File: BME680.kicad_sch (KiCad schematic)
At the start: 19 parts, among them IC1 BME680, J3 HEADER-1X770MIL, Q1 BSS138, U3 AP2112K-3.3

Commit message: added Arduino UNO R4 in root sheet
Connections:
- net D6 renamed CS
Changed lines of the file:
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@@
 		)
 	)
-	(hierarchical_label "D6"
+	(hierarchical_label "CS"
 		(shape input)
 		(at 68.58 133.35 180)

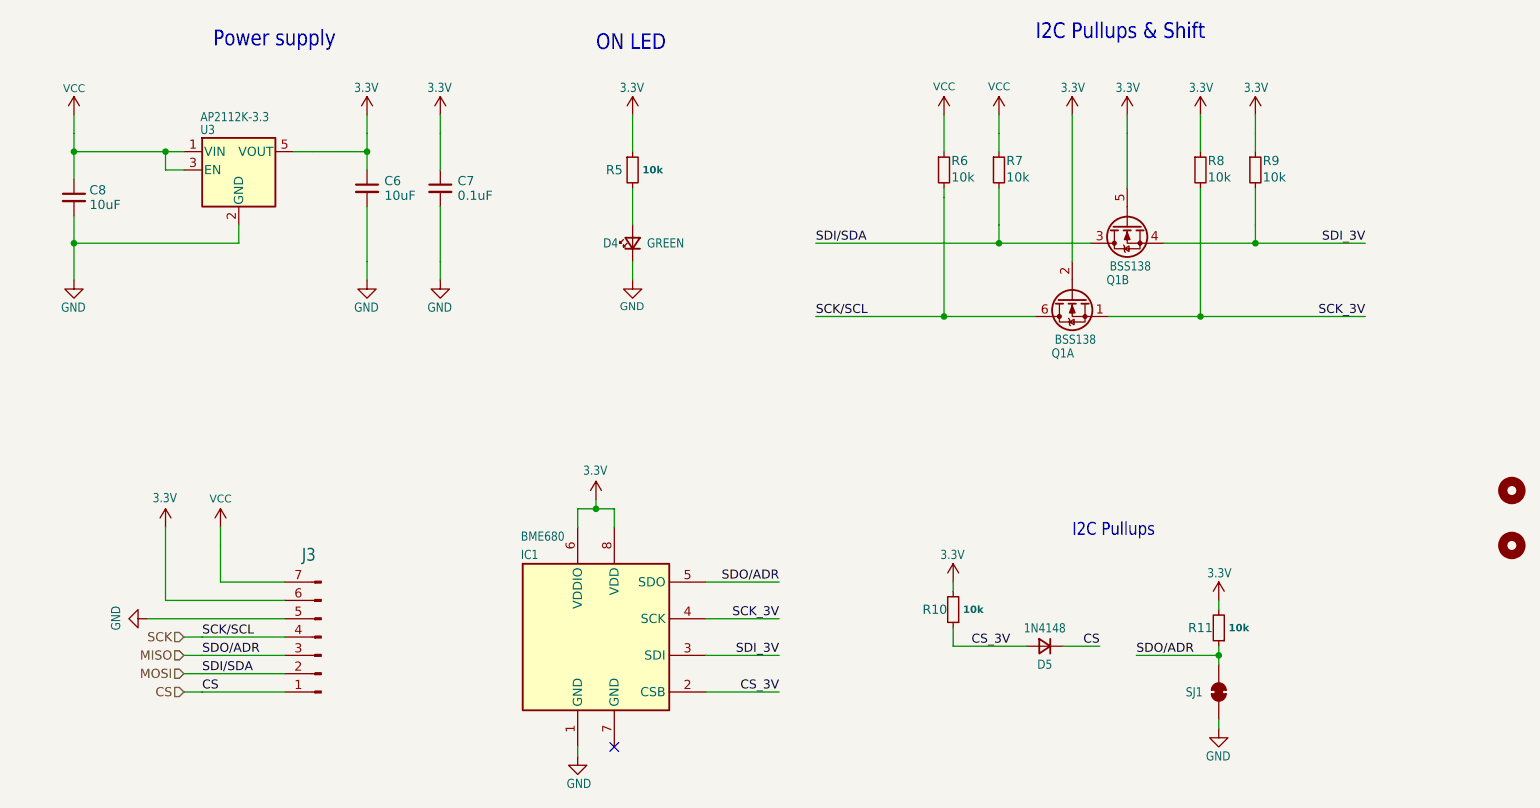
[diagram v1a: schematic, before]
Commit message: added pyrano, anemo, AM2315C, power supply, LEDs, switch and FPC connector in schematic
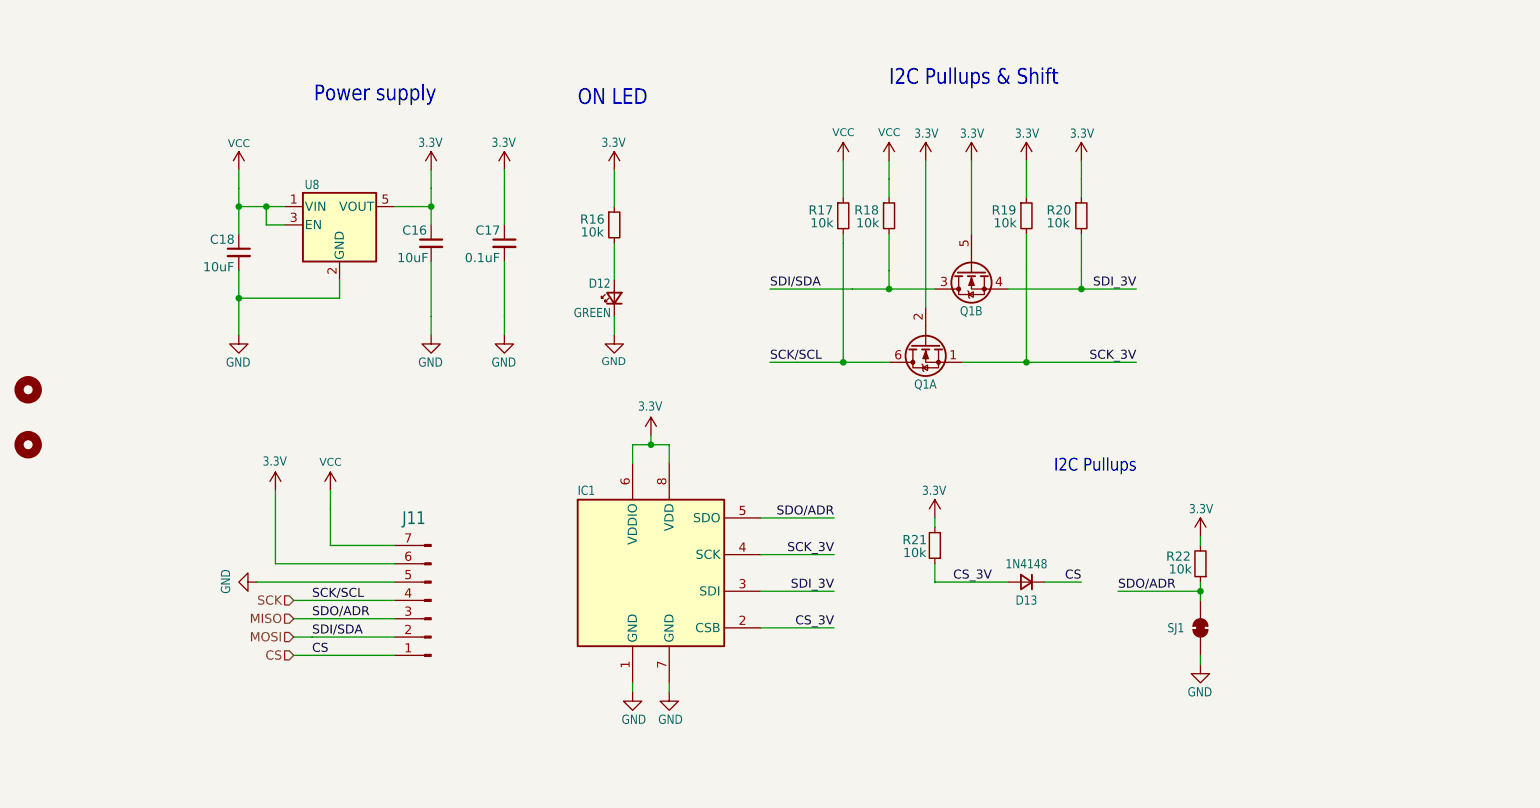
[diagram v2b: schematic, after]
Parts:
- C16: renamed from C6; Componant package type C_0805 -> (none); Component package type (none) -> C_0805
- C17: renamed from C7; Componant package type C_0603 -> (none); Component package type (none) -> C_0603
- C18: renamed from C8; Componant package type C_0805 -> (none); Component package type (none) -> C_0805
- D12: renamed from D4; Componant package type LED_0603 -> (none); Component package type (none) -> LED_0603
- D13: renamed from D5; Componant package type SOD-323 -> (none); Component package type (none) -> SOD-323
- IC1: Componant package type / -> (none)
- J11: renamed from J3; Componant package type / -> (none)
- Q1: Componant package type SOT-363 -> (none); Component package type (none) -> SOT-363
- R16: renamed from R5; Componant package type R_0603 -> (none); Component package type (none) -> R_0603
- R17: renamed from R6; Componant package type R_0603 -> (none); Component package type (none) -> R_0603
- R18: renamed from R7; Componant package type R_0603 -> (none); Component package type (none) -> R_0603
- R19: renamed from R8; Componant package type R_0603 -> (none); Component package type (none) -> R_0603
- R20: renamed from R9; Componant package type R_0603 -> (none); Component package type (none) -> R_0603
- R21: renamed from R10; Componant package type R_0603 -> (none); Component package type (none) -> R_0603
- R22: renamed from R11; Componant package type R_0603 -> (none); Component package type (none) -> R_0603
- U8: renamed from U3; Componant package type SOT-25 -> (none); Component package type (none) -> SOT-25
- renumbered U$3 to U$7, U$4 to U$8
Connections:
- net GND: now also IC1.7 (GND)
- no-connect marks 1 -> 0
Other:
- moved on the sheet: C16, C17, C18, D12, D13, IC1, J11, Q1A, Q1B, R16, R17, R18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

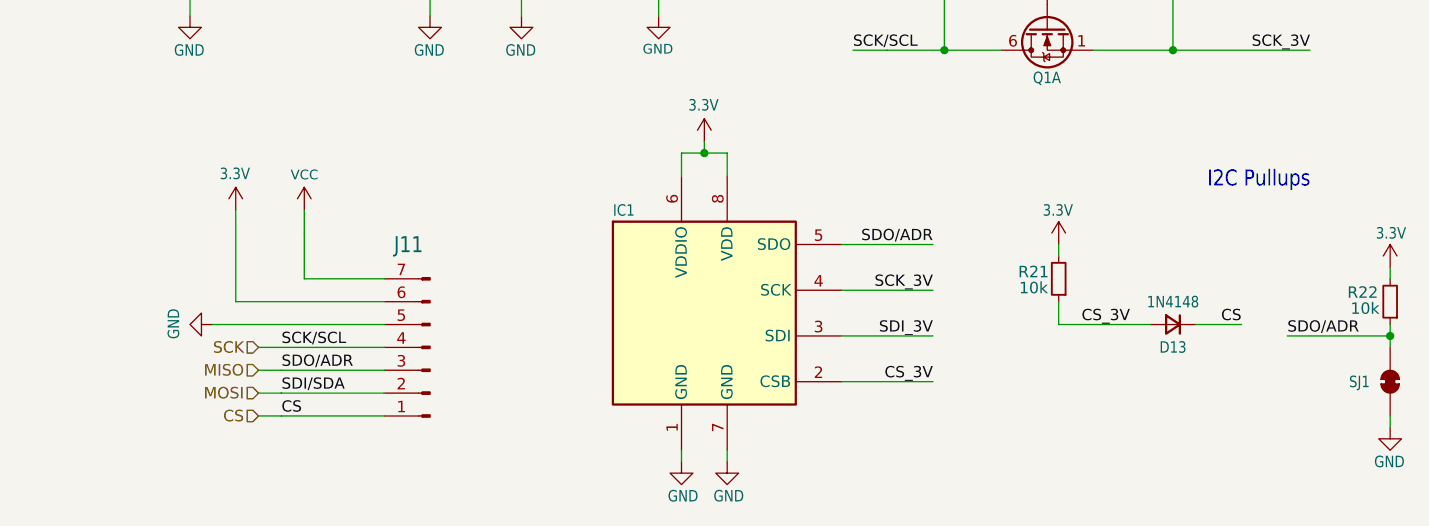
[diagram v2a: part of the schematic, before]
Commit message: removed connectors from modules
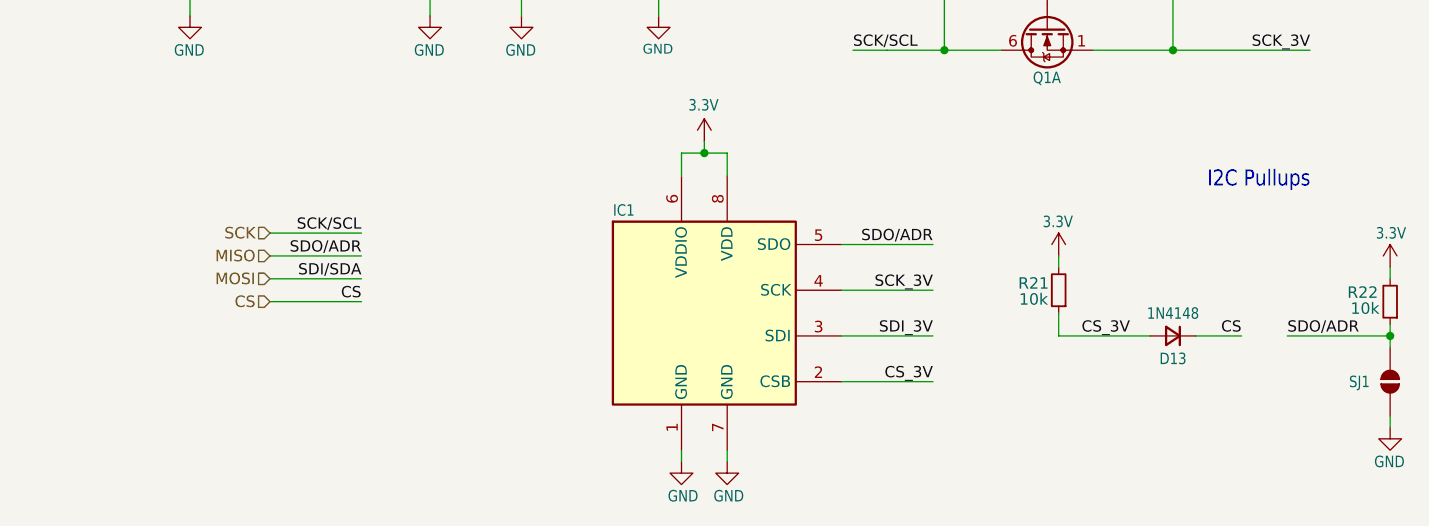
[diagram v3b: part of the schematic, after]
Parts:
- removed J11: HEADER-1X770MIL, Connector_PinHeader_2.54mm:PinHeader_1x07_P2.54mm_Vertical, symbol Connector:Conn_01x07_Pin
- SJ1: symbol Jumper:SolderJumper_2_Bridged -> Jumper:SolderJumper_2_Open
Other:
- moved on the sheet: D13, R21

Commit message: removed mouting holes
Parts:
- removed U$7, U$8: MOUNTINGHOLE2.5, MountingHole:MountingHole_2.5mm, symbol Mechanical:MountingHole
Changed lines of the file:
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@@
-	)
-	(symbol
-		(lib_id "Mechanical:MountingHole")
-		(at 46.99 91.44 0)
-		(unit 1)
-		(exclude_from_sim yes)
-		(in_bom no)
-		(on_board yes)
-		(dnp no)
-		(property "Reference" "U$7"
-			(at 46.99 91.44 0)
-			(effects
-				(font
-					(size 1.27 1.27)
-				)
-				(hide yes)
-			)
-		)
-		(property "Value" "MOUNTINGHOLE2.5"
-			(at 46.99 91.44 0)
-			(effects
-				(font
-					(size 1.27 1.27)
-				)
-				(hide yes)
-			)
-		)
-		(property "Footprint" "MountingHole:MountingHole_2.5mm"
-			(at 46.99 91.44 0)
-			(effects
-				(font
-					(size 1.27 1.27)
-				)
-				(hide yes)
-			)
-		)
-		(property "Datasheet" "~"
-			(at 46.99 91.44 0)
-			(effects
-				(font
-					(size 1.27 1.27)
-				)
-				(hide yes)
-			)
-		)
-		(property "Description" "Mounting Hole without connection"
-			(at 46.99 91.44 0)
-			(effects
-				(font
-					(size 1.27 1.27)
-				)
-				(hide yes)
-			)
-		)
-		(property "MPN" ""
-			(at 46.99 91.44 0)
-			(effects
-				(font
-					(size 1.27 1.27)
-				)
-				(hide yes)
-			)
-		)
-		(property "Manufacturer" ""
-			(at 46.99 91.44 0)
-			(effects
-				(font
-					(size 1.27 1.27)
-				)
-				(hide yes)
-			)
-		)
-		(property "SPN" ""
-			(at 46.99 91.44 0)
-			(effects
-				(font
-					(size 1.27 1.27)
-				)
-				(hide yes)
-			)
-		)
-		(property "Supplier" ""
-			(at 46.99 91.44 0)
-			(effects
-				(font
-					(size 1.27 1.27)
-				)
-				(hide yes)
-			)
-		)
-		(instances
-			(project "testing-station"
-				(path "/ed3950ec-e24f-4dd6-b9cc-eca012f1333b/7e22e2c2-9f9e-4784-92a8-ea554e7deb4d"
-					(reference "U$7")
-					(unit 1)
-				)
-			)
-		)
 	)
 	(symbol
@@
 					(unit 1)
 				)
-			)
-		)
-	)
-	(symbol
-		(lib_id "Mechanical:MountingHole")
-		(at 46.99 99.06 0)
-		(unit 1)
-		(exclude_from_sim yes)
-		(in_bom no)
-		(on_board yes)
-		(dnp no)
-		(property "Reference" "U$8"
-			(at 46.99 99.06 0)
-			(effects
-				(font
-					(size 1.27 1.27)
-				)
-				(hide yes)
-			)
-		)
-		(property "Value" "MOUNTINGHOLE2.5"
-			(at 46.99 99.06 0)
-			(effects
-				(font
-					(size 1.27 1.27)
-				)
-				(hide yes)
-			)
-		)
-		(property "Footprint" "MountingHole:MountingHole_2.5mm"
-			(at 46.99 99.06 0)
-			(effects
-				(font
-					(size 1.27 1.27)
-				)
-				(hide yes)
-			)
-		)
-		(property "Datasheet" "~"
-			(at 46.99 99.06 0)
-			(effects
-				(font
-					(size 1.27 1.27)
-				)
-				(hide yes)
-			)
-		)
-		(property "Description" "Mounting Hole without connection"
-			(at 46.99 99.06 0)
-			(effects
-				(font
-					(size 1.27 1.27)
-				)
-				(hide yes)
-			)
-		)
-		(property "MPN" ""
-			(at 46.99 99.06 0)
-			(effects
-				(font
-					(size 1.27 1.27)
-				)
-				(hide yes)
-			)
-		)
-		(property "Manufacturer" ""
-			(at 46.99 99.06 0)
-			(effects
-				(font
-					(size 1.27 1.27)
-				)
-				(hide yes)
-			)
-		)
-		(property "SPN" ""
-			(at 46.99 99.06 0)
-			(effects
-				(font
-					(size 1.27 1.27)
-				)
-				(hide yes)
-			)
-		)
-		(property "Supplier" ""
-			(at 46.99 99.06 0)
-			(effects
-				(font
-					(size 1.27 1.27)
-				)
-				(hide yes)
-			)
-		)
-		(instances
-			(project "testing-station"
-				(path "/ed3950ec-e24f-4dd6-b9cc-eca012f1333b/7e22e2c2-9f9e-4784-92a8-ea554e7deb4d"
-					(reference "U$8")
-					(unit 1)
-				)

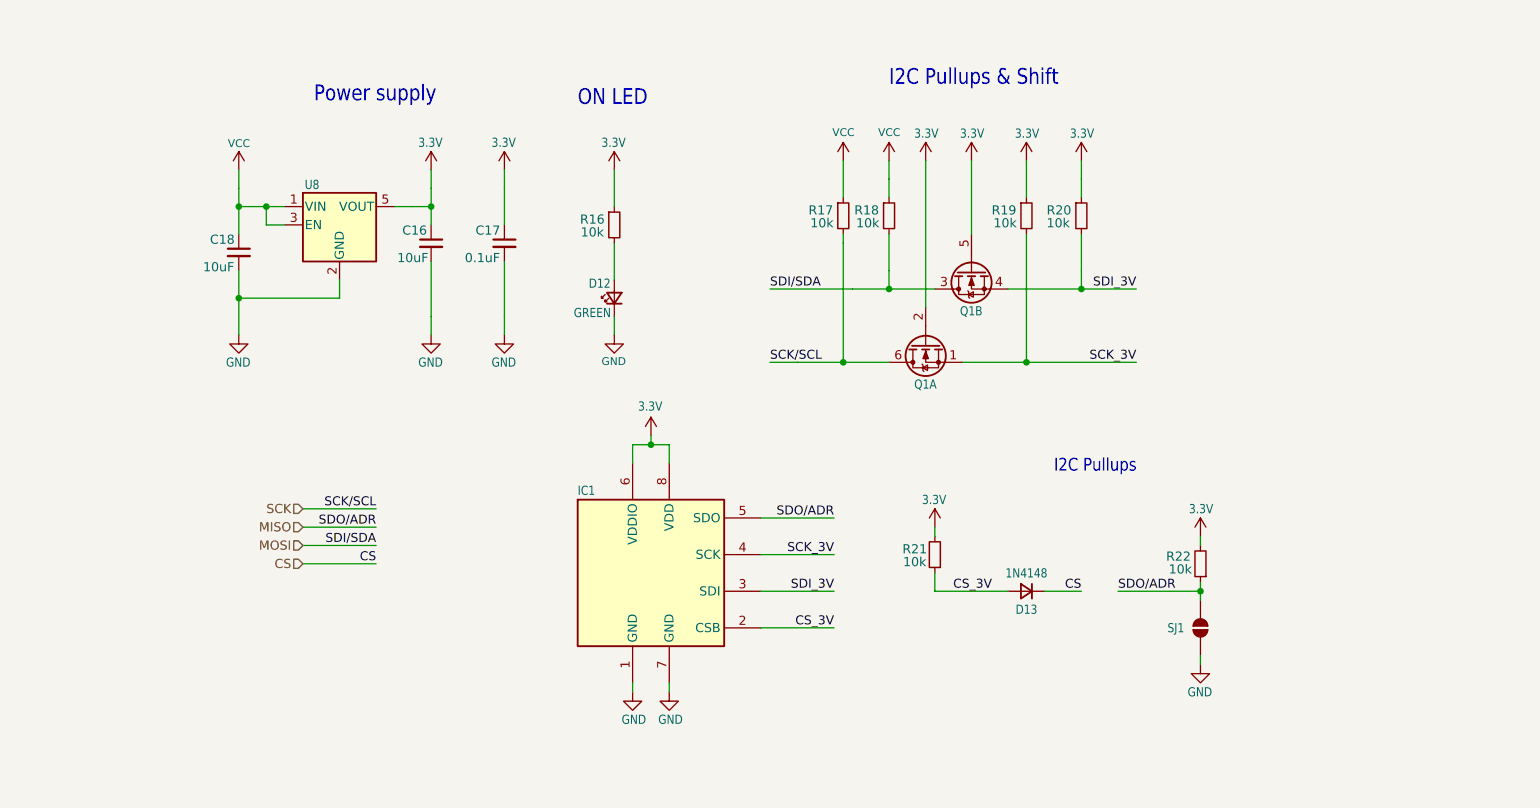
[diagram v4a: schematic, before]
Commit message: removed voltage regulators of each individual module
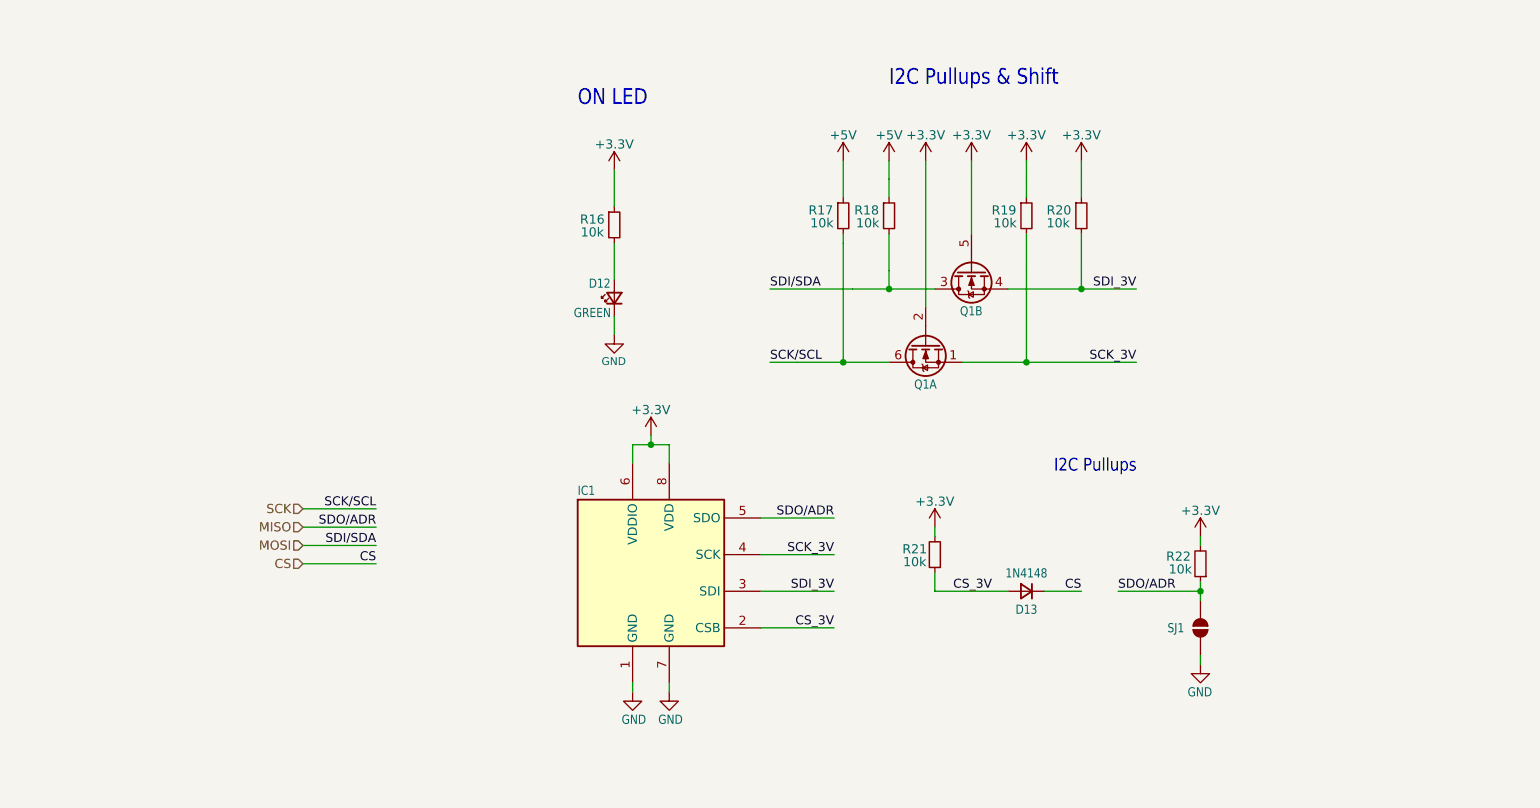
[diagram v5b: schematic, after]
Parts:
- removed C16, C18: 10uF, Capacitor_SMD:C_0805_2012Metric, symbol Device:C_Small
- removed C17: 0.1uF, Capacitor_SMD:C_0603_1608Metric, symbol Device:C_Small
- removed U8: AP2112K-3.3, Package_TO_SOT_SMD:SOT-23-5, symbol Regulator_Linear:AP2112K-3.3
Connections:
- net 3.3V renamed +3.3V
- net VCC renamed +5V
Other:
- note removed: "Power supply"

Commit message: BOM update
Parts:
- D12: Component package type LED_0603 -> (none)
- D13: Component package type SOD-323 -> (none)
- Q1: Component package type SOT-363 -> (none)
- R16, R17, R18, R19, R20, R21, R22: Component package type R_0603 -> (none)
- renumbered SJ1 to JP10
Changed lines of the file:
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@@
-			)
-		)
-		(property "Component package type" "R_0603"
-			(at 128.27 68.58 0)
-			(effects
-				(font
-					(size 1.27 1.27)
-				)
-				(hide yes)
 			)
 		)
@@
 			)
 		)
-		(property "Component package type" "R_0603"
-			(at 160.02 67.31 0)
-			(effects
-				(font
-					(size 1.27 1.27)
-				)
-				(hide yes)
-			)
-		)
 		(pin "1"
 		)
@@
 		(on_board yes)
 		(dnp no)
-		(property "Reference" "SJ1"
-			(at 204.978 125.222 90)
+		(property "Reference" "JP10"
+			(at 203.962 125.222 90)
 			(effects
 				(font
@@
 			(project "testing-station"
 				(path "/ed3950ec-e24f-4dd6-b9cc-eca012f1333b/7e22e2c2-9f9e-4784-92a8-ea554e7deb4d"
-					(reference "SJ1")
+					(reference "JP10")
 					(unit 1)
 				)
@@
 			)
 		)
-		(property "Component package type" "SOT-363"
-			(at 171.45 85.09 0)
-			(effects
-				(font
-					(size 1.27 1.27)
-				)
-				(hide yes)
-			)
-		)
 		(pin "1"
 		)
@@
 			)
 		)
-		(property "Component package type" "R_0603"
-			(at 172.72 114.3 0)
-			(effects
-				(font
-					(size 1.27 1.27)
-				)
-				(hide yes)
-			)
-		)
 		(pin "1"
 		)
@@
 		)
 		(property "Supplier" "Eurocircuits"
-			(at 209.55 115.57 0)
-			(effects
-				(font
-					(size 1.27 1.27)
-				)
-				(hide yes)
-			)
-		)
-		(property "Component package type" "R_0603"
 			(at 209.55 115.57 0)
 			(effects
@@
 			)
 		)
-		(property "Component package type" "SOT-363"
-			(at 177.8 74.93 0)
-			(effects
-				(font
-					(size 1.27 1.27)
-				)
-				(hide yes)
-			)
-		)
 		(pin "1"
 		)
@@
 			)
 		)
-		(property "Component package type" "LED_0603"
-			(at 128.27 78.74 0)
-			(effects
-				(font
-					(size 1.27 1.27)
-				)
-				(hide yes)
-			)
-		)
 		(pin "1"
 		)
@@
 			)
 		)
-		(property "Component package type" "R_0603"
-			(at 185.42 67.31 0)
-			(effects
-				(font
-					(size 1.27 1.27)
-				)
-				(hide yes)
-			)
-		)
 		(pin "1"
 		)
@@
 			)
 		)
-		(property "Component package type" "R_0603"
-			(at 193.04 67.31 0)
-			(effects
-				(font
-					(size 1.27 1.27)
-				)
-				(hide yes)
-			)
-		)
 		(pin "1"
 		)
@@
 			)
 		)
-		(property "Component package type" "R_0603"
-			(at 166.37 67.31 0)
-			(effects
-				(font
-					(size 1.27 1.27)
-				)
-				(hide yes)
-			)
-		)
 		(pin "1"
 		)
@@
 			(at 185.42 119.38 0)
 			(effects
-				(font
-					(size 1.27 1.27)
-				)
-				(hide yes)
-			)
-		)
-		(property "Component package type" "SOD-323"
-			(at 185.42 119.38 0)
-			(effects
